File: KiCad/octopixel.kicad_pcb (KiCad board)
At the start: 2 copper layers, 25.8 x 35.5 mm, 8 parts, among them J2 RBG PB3, J3 RBG PB4, J4 RBG PB5, J5 RBG_PB3, J6 Octopus SPI3, U1 CD4050BE

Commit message: Intial commit for SMD version
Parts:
- removed H1, H2: MountingHole, MountingHole:MountingHole_3.2mm_M3_DIN965_Pad
- removed J2: RBG PB3, Connector_JST:JST_XH_B3B-XH-AM_1x03_P2.50mm_Vertical
- removed J3: RBG PB4, Connector_JST:JST_XH_B3B-XH-AM_1x03_P2.50mm_Vertical
- removed J4: RBG PB5, Connector_JST:JST_XH_B3B-XH-AM_1x03_P2.50mm_Vertical
- removed J5: RBG_PB3, Connector_JST:JST_XH_B3B-XH-AM_1x03_P2.50mm_Vertical
- removed U1: CD4050BE, easyeda:DIP-16_L20.3-W10.2-P2.54-LS10.2-BL
- added CN5: PH2.0-3PWB Horizontal, easyeda:CONN-TH_PH-3PWB, F.Cu at (94.6, 37.4)
- added CN6: PH2.0-3PWB Horizontal, easyeda:CONN-TH_PH-3PWB, F.Cu at (94.6, 61.1)
- added CN7: PH2.0-3PWB Horizontal, easyeda:CONN-TH_PH-3PWB, B.Cu at (94.6, 37.4)
- added CN8: PH2.0-3PWB Horizontal, easyeda:CONN-TH_PH-3PWB, B.Cu at (94.6, 61.1)
- added U2: TXS0104EPWR, easyeda:TSSOP-14_L5.0-W4.4-P0.65-LS6.4-BL, F.Cu at (89.5, 48.3)
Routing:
- net +3V3: track 0.00 -> 32.7 mm, vias 0 -> 1
- net +5V: track 55.6 -> 63.7 mm, vias 0 -> 4
- net PB5: track 12.3 -> 19.6 mm
- net PA15_{5V}: track 10.7 -> 16.4 mm
- net PB3_{5V}: track 21.2 -> 26.6 mm
- net PA15: track 15.1 -> 11.0 mm
- net PB3: track 14.9 -> 18.2 mm
- net PB4: track 10.1 -> 6.85 mm
- net PB4_{5V}: track 15.3 -> 18.1 mm, vias 0 -> 1
- net GND: track 0.00 -> 2.50 mm, vias 0 -> 1
- net PB5_{5V}: track 12.5 -> 10.8 mm, vias 0 -> 1
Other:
- board size 25.8 x 35.5 mm -> 16 x 35.6 mm
- board text added: "OctoPix SMD"
- board text added: "PA15"
- board text removed: "OctoPix"
- board text removed: "PB15"

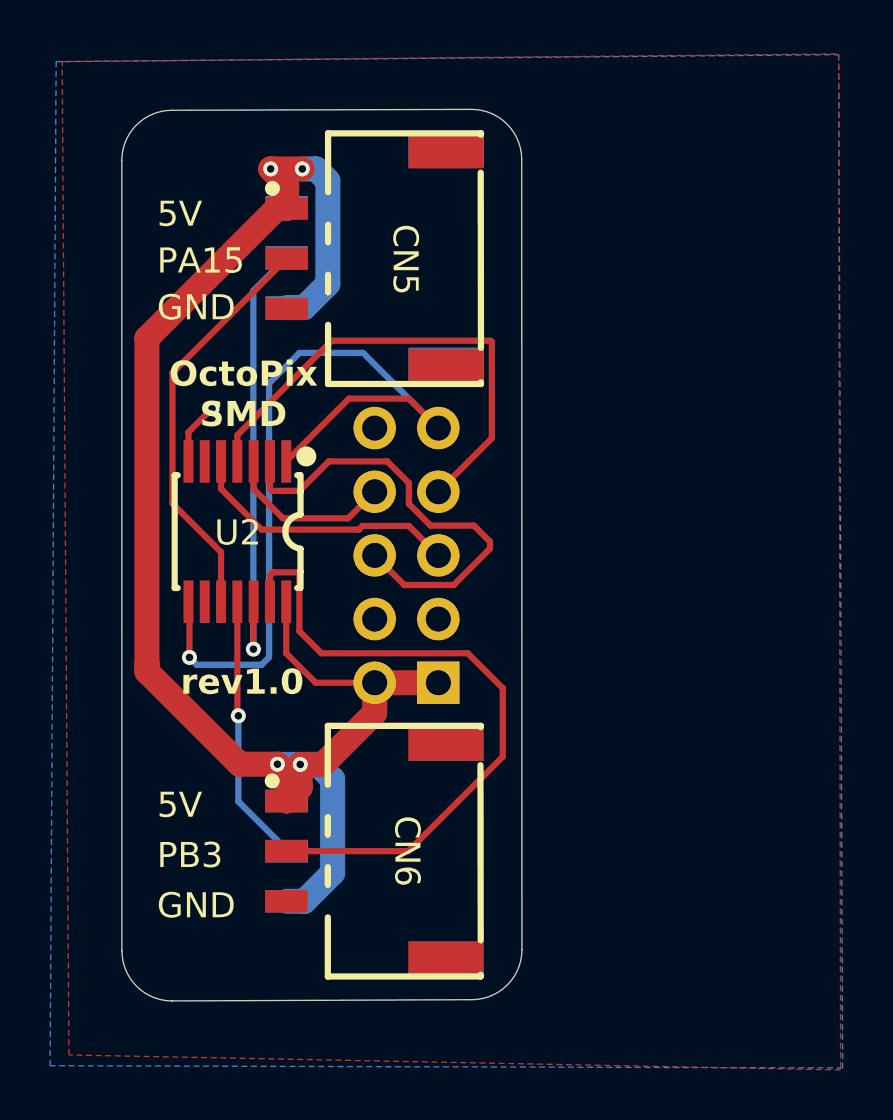
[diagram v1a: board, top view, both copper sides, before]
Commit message: Included missing grounds for connectors
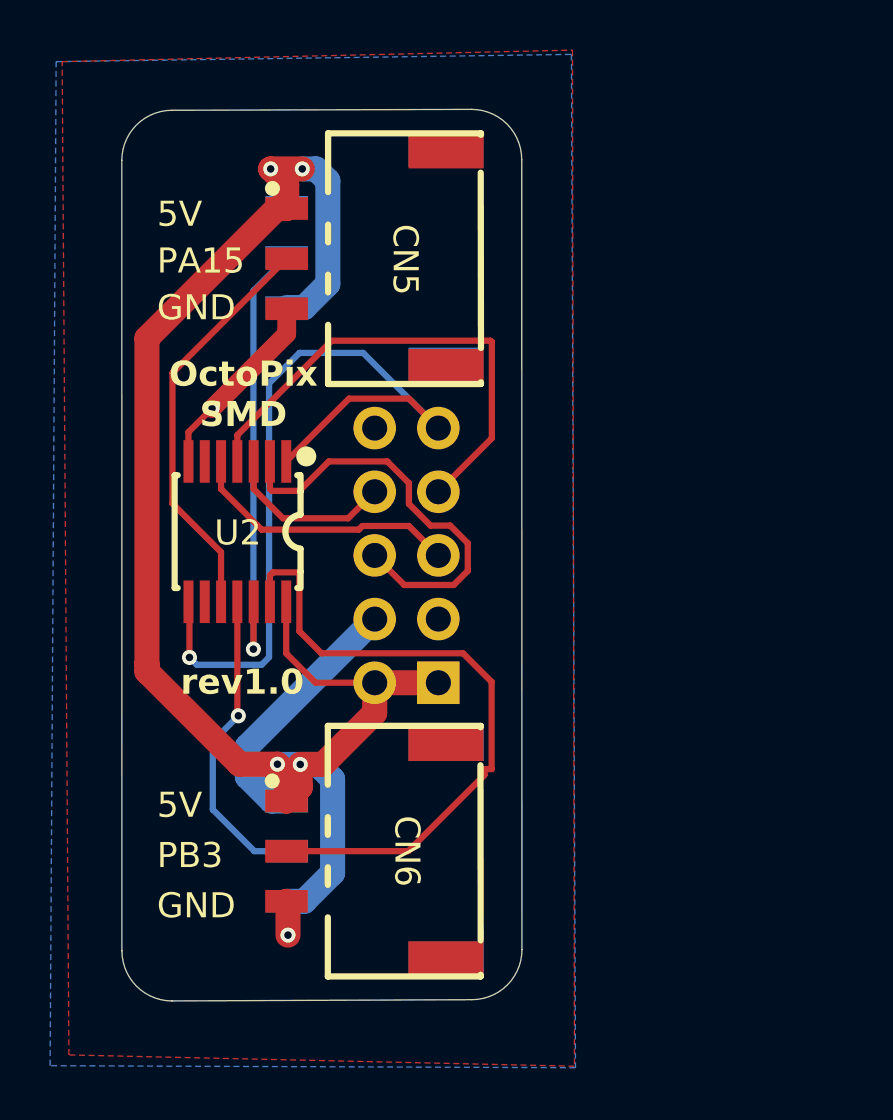
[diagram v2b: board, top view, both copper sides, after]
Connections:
- CN5 pad 3: unconnected-(CN5-Pad3) -> GND
- CN6 pad 3: unconnected-(CN6-Pad3) -> GND
- CN7 pad 3: unconnected-(CN7-Pad3) -> GND
- CN8 pad 3: unconnected-(CN8-Pad3) -> GND
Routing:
- net GND: track 2.50 -> 19.5 mm, vias 1 -> 2
- net PB5_{5V}: track 10.8 -> 12.4 mm
- net PB3: track 18.2 -> 16.9 mm
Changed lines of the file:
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@@
 	(net 13 "unconnected-(U2-NC-Pad9)")
 	(net 14 "unconnected-(CN5-Pad0)")
-	(net 15 "unconnected-(CN5-Pad3)")
-	(net 16 "unconnected-(CN5-Pad0)_0")
-	(net 17 "unconnected-(CN6-Pad3)")
-	(net 18 "unconnected-(CN6-Pad0)")
-	(net 19 "unconnected-(CN6-Pad0)_0")
-	(net 20 "unconnected-(CN7-Pad3)")
-	(net 21 "unconnected-(CN7-Pad0)")
-	(net 22 "unconnected-(CN7-Pad0)_0")
-	(net 23 "unconnected-(CN8-Pad3)")
-	(net 24 "unconnected-(CN8-Pad0)")
-	(net 25 "unconnected-(CN8-Pad0)_0")
+	(net 15 "unconnected-(CN5-Pad0)_0")
+	(net 16 "unconnected-(CN6-Pad0)")
+	(net 17 "unconnected-(CN6-Pad0)_0")
+	(net 18 "unconnected-(CN7-Pad0)")
+	(net 19 "unconnected-(CN7-Pad0)_0")
+	(net 20 "unconnected-(CN8-Pad0)")
+	(net 21 "unconnected-(CN8-Pad0)_0")
 	(footprint "easyeda:TSSOP-14_L5.0-W4.4-P0.65-LS6.4-BL"
 		(layer "F.Cu")
@@
 			(size 1.3 3)
 			(layers "F.Cu" "F.Paste" "F.Mask")
-			(net 16 "unconnected-(CN5-Pad0)_0")
+			(net 15 "unconnected-(CN5-Pad0)_0")
 			(pinfunction "0")
 			(pintype "unspecified+no_connect")
@@
 			(size 0.9 1.7)
 			(layers "F.Cu" "F.Paste" "F.Mask")
-			(net 15 "unconnected-(CN5-Pad3)")
+			(net 1 "GND")
 			(pinfunction "3")
-			(pintype "input+no_connect")
+			(pintype "input")
 		)
 		(model "easyeda.3dshapes/CONN-TH_PH-3PWB.wrl"
@@
 			(size 1.3 3)
 			(layers "F.Cu" "F.Paste" "F.Mask")
-			(net 19 "unconnected-(CN6-Pad0)_0")
+			(net 17 "unconnected-(CN6-Pad0)_0")
 			(pinfunction "0")
 			(pintype "unspecified+no_connect")
@@
 			(size 1.3 3)
 			(layers "F.Cu" "F.Paste" "F.Mask")
-			(net 18 "unconnected-(CN6-Pad0)")
+			(net 16 "unconnected-(CN6-Pad0)")
 			(pinfunction "0")
 			(pintype "unspecified+no_connect")
@@
 			(size 0.9 1.7)
 			(layers "F.Cu" "F.Paste" "F.Mask")
-			(net 17 "unconnected-(CN6-Pad3)")
+			(net 1 "GND")
 			(pinfunction "3")
-			(pintype "input+no_connect")
+			(pintype "input")
 		)
 		(model "easyeda.3dshapes/CONN-TH_PH-3PWB.wrl"
@@
 		)
 		(property "Value" "PH2.0-3PWB Horizontal"
-			(at 0 -7.18 270)
+			(at 0 -7.18 -90)
 			(layer "B.Fab")
 			(effects
@@
 		)
 		(fp_text user "${REFERENCE}"
-			(at 0 0 270)
+			(at 0 0 -90)
 			(layer "B.Fab")
 			(effects
@@
 			(size 1.3 3)
 			(layers "B.Cu" "B.Paste" "B.Mask")
-			(net 21 "unconnected-(CN7-Pad0)")
+			(net 18 "unconnected-(CN7-Pad0)")
 			(pinfunction "0")
 			(pintype "unspecified+no_connect")
@@
 			(size 1.3 3)
 			(layers "B.Cu" "B.Paste" "B.Mask")
-			(net 22 "unconnected-(CN7-Pad0)_0")
+			(net 19 "unconnected-(CN7-Pad0)_0")
 			(pinfunction "0")
 			(pintype "unspecified+no_connect")
@@
 			(size 0.9 1.7)
 			(layers "B.Cu" "B.Paste" "B.Mask")
-			(net 20 "unconnected-(CN7-Pad3)")
+			(net 1 "GND")
 			(pinfunction "3")
-			(pintype "input+no_connect")
+			(pintype "input")
 		)
 		(model "easyeda.3dshapes/CONN-TH_PH-3PWB.wrl"
@@
 		)
 		(property "Value" "PH2.0-3PWB Horizontal"
-			(at 0 -7.18 270)
+			(at 0 -7.18 -90)
 			(layer "B.Fab")
 			(effects
@@
 		)
 		(fp_text user "${REFERENCE}"
-			(at 0 0 270)
+			(at 0 0 -90)
 			(layer "B.Fab")
 			(effects
@@
 			(size 1.3 3)
 			(layers "B.Cu" "B.Paste" "B.Mask")
-			(net 24 "unconnected-(CN8-Pad0)")
+			(net 20 "unconnected-(CN8-Pad0)")
 			(pinfunction "0")
 			(pintype "unspecified+no_connect")
@@
 			(size 1.3 3)
 			(layers "B.Cu" "B.Paste" "B.Mask")
-			(net 25 "unconnected-(CN8-Pad0)_0")
+			(net 21 "unconnected-(CN8-Pad0)_0")
 			(pinfunction "0")
 			(pintype "unspecified+no_connect")
@@
 			(size 0.9 1.7)
 			(layers "B.Cu" "B.Paste" "B.Mask")
-			(net 23 "unconnected-(CN8-Pad3)")
+			(net 1 "GND")
 			(pinfunction "3")
-			(pintype "input+no_connect")
+			(pintype "input")
 		)
 		(model "easyeda.3dshapes/CONN-TH_PH-3PWB.wrl"
@@
 	)
 	(segment
+		(start 91.48 63.14)
+		(end 91.42 63.08)
+		(width 1)
+		(layer "F.Cu")
+		(net 1)
+	)
+	(segment
+		(start 91.43 40.44)
+		(end 88.45 43.42)
+		(width 0.75)
+		(layer "F.Cu")
+		(net 1)
+	)
+	(segment
+		(start 91.43 39.44)
+		(end 91.43 40.44)
+		(width 0.75)
+		(layer "F.Cu")
+		(net 1)
+	)
+	(segment
+		(start 91.48 64.43)
+		(end 91.48 63.14)
+		(width 1)
+		(layer "F.Cu")
+		(net 1)
+	)
+	(segment
 		(start 87.51 44.36)
 		(end 88.45 43.42)
@@
 		(net 1)
 	)
+	(via
+		(at 91.48 64.43)
+		(size 0.6)
+		(drill 0.3)
+		(layers "F.Cu" "B.Cu")
+		(free yes)
+		(net 1)
+	)
+	(segment
+		(start 89.86 56.9)
+		(end 94.94 51.82)
+		(width 1)
+		(layer "B.Cu")
+		(net 1)
+	)
+	(segment
+		(start 90.832944 59.08)
+		(end 89.86 58.107056)
+		(width 1)
+		(layer "B.Cu")
+		(net 1)
+	)
+	(segment
+		(start 89.86 58.107056)
+		(end 89.86 56.9)
+		(width 1)
+		(layer "B.Cu")
+		(net 1)
+	)
+	(segment
+		(start 91.43 59.08)
+		(end 90.832944 59.08)
+		(width 1)
+		(layer "B.Cu")
+		(net 1)
+	)
 	(segment
 		(start 93.88 47.8)
@@
 	)
 	(segment
-		(start 90.76 45.53)
-		(end 90.76 46.63)
+		(start 97.951701 48.09)
+		(end 98.655 48.793299)
 		(width 0.25)
 		(layer "F.Cu")
@@
 	)
 	(segment
-		(start 98.9 48.09)
-		(end 99.54 48.73)
+		(start 96.305 46.395)
+		(end 96.305 47.226701)
 		(width 0.25)
 		(layer "F.Cu")
@@
 	)
 	(segment
-		(start 91.935 46.705)
-		(end 93.11 45.53)
+		(start 90.76 46.63)
+		(end 90.835 46.705)
 		(width 0.25)
 		(layer "F.Cu")
@@
 	)
 	(segment
-		(start 90.835 46.705)
-		(end 91.935 46.705)
+		(start 96.12 50.46)
+		(end 94.94 49.28)
 		(width 0.25)
 		(layer "F.Cu")
@@
 	)
 	(segment
-		(start 97.168299 48.09)
-		(end 98.9 48.09)
+		(start 98.09 50.46)
+		(end 96.12 50.46)
 		(width 0.25)
 		(layer "F.Cu")
@@
 	)
 	(segment
-		(start 98.09 50.46)
-		(end 96.12 50.46)
+		(start 90.76 45.53)
+		(end 90.76 46.63)
 		(width 0.25)
 		(layer "F.Cu")
@@
 	)
 	(segment
-		(start 99.54 48.73)
-		(end 99.54 49.01)
+		(start 90.835 46.705)
+		(end 91.935 46.705)
 		(width 0.25)
 		(layer "F.Cu")
@@
 	)
 	(segment
-		(start 95.44 45.53)
-		(end 96.305 46.395)
+		(start 97.168299 48.09)
+		(end 97.951701 48.09)
 		(width 0.25)
 		(layer "F.Cu")
@@
 	)
 	(segment
-		(start 90.76 46.63)
-		(end 90.835 46.705)
+		(start 95.44 45.53)
+		(end 96.305 46.395)
 		(width 0.25)
 		(layer "F.Cu")
@@
 	)
 	(segment
-		(start 99.54 49.01)
+		(start 98.655 49.895)
 		(end 98.09 50.46)
 		(width 0.25)
@@
 	)
 	(segment
-		(start 96.305 46.395)
-		(end 96.305 47.226701)
+		(start 91.935 46.705)
+		(end 93.11 45.53)
 		(width 0.25)
 		(layer "F.Cu")
@@
 	)
 	(segment
-		(start 96.12 50.46)
-		(end 94.94 49.28)
+		(start 98.655 48.793299)
+		(end 98.655 49.895)
 		(width 0.25)
 		(layer "F.Cu")
@@
 	)
 	(segment
-		(start 98.655 53.185)
-		(end 100.05 54.58)
+		(start 91.935 49.955)
+		(end 91.935 52.305)
 		(width 0.25)
 		(layer "F.Cu")
@@
 	)
 	(segment
+		(start 99.32 57.805)
+		(end 99.32 58.04)
+		(width 0.25)
+		(layer "F.Cu")
+		(net 7)
+	)
+	(segment
+		(start 90.885 49.955)
+		(end 91.935 49.955)
+		(width 0.25)
+		(layer "F.Cu")
+		(net 7)
+	)
+	(segment
 		(start 92.815 53.185)
-		(end 98.655 53.185)
+		(end 98.465 53.185)
 		(width 0.25)
 		(layer "F.Cu")
@@
 	)
 	(segment
-		(start 100.05 54.58)
-		(end 100.05 57.31)
+		(start 99.605 57.805)
+		(end 99.32 57.805)
 		(width 0.25)
 		(layer "F.Cu")
@@
 	)
 	(segment
-		(start 91.935 52.305)
-		(end 92.815 53.185)
+		(start 99.32 58.04)
+		(end 96.28 61.08)
 		(width 0.25)
 		(layer "F.Cu")
@@
 	)
 	(segment
-		(start 96.28 61.08)
-		(end 91.42 61.08)
+		(start 99.605 54.325)
+		(end 99.605 57.805)
 		(width 0.25)
 		(layer "F.Cu")
@@
 	)
 	(segment
-		(start 90.885 49.955)
-		(end 91.935 49.955)
+		(start 91.935 52.305)
+		(end 92.815 53.185)
 		(width 0.25)
 		(layer "F.Cu")
@@
 	)
 	(segment
-		(start 91.935 49.955)
-		(end 91.935 52.305)
+		(start 96.28 61.08)
+		(end 91.42 61.08)
 		(width 0.25)
 		(layer "F.Cu")
@@
 	)
 	(segment
-		(start 100.05 57.31)
-		(end 96.28 61.08)
+		(start 98.465 53.185)
+		(end 99.605 54.325)
 		(width 0.25)
 		(layer "F.Cu")
@@
 	)
 	(segment
-		(start 89.5 59.1)
-		(end 91.43 61.03)
+		(start 89.5 55.68)
+		(end 88.48 56.7)
 		(width 0.25)
 		(layer "B.Cu")
@@
 	)
 	(segment
-		(start 91.43 61.03)
-		(end 91.43 61.08)
+		(start 88.48 56.7)
+		(end 88.48 59.42)
 		(width 0.25)
 		(layer "B.Cu")
@@
 	)
 	(segment
-		(start 89.5 55.68)
-		(end 89.5 59.1)
+		(start 88.48 59.42)
+		(end 90.14 61.08)
+		(width 0.25)
+		(layer "B.Cu")
+		(net 9)
+	)
+	(segment
+		(start 90.14 61.08)
+		(end 91.43 61.08)
 		(width 0.25)
 		(layer "B.Cu")
@@
 		(polygon
 			(pts
-				(xy 82.47 29.58) (xy 113.45 29.27) (xy 113.53 69.81) (xy 82.74 69.21)
+				(xy 82.47 29.58) (xy 102.83 29.12) (xy 102.91 69.66) (xy 82.74 69.21)
 			)
 		)
@@
 		(polygon
 			(pts
-				(xy 82.23 29.58) (xy 113.45 29.3) (xy 113.61 69.73) (xy 81.99 69.64)
+				(xy 82.23 29.58) (xy 102.79 29.29) (xy 102.95 69.72) (xy 81.99 69.64)
 			)
 		)
